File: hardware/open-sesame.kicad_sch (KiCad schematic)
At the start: 33 parts, among them J1 Conn_01x02, J2 Conn_01x06, J3 Conn_01x02, J4 Conn_01x02, J5 Conn_01x02, J6 Conn_01x02, J7 Qwiic_RA, U1 CPC1019N, U2 CPC1019N, U3 CPC1019N

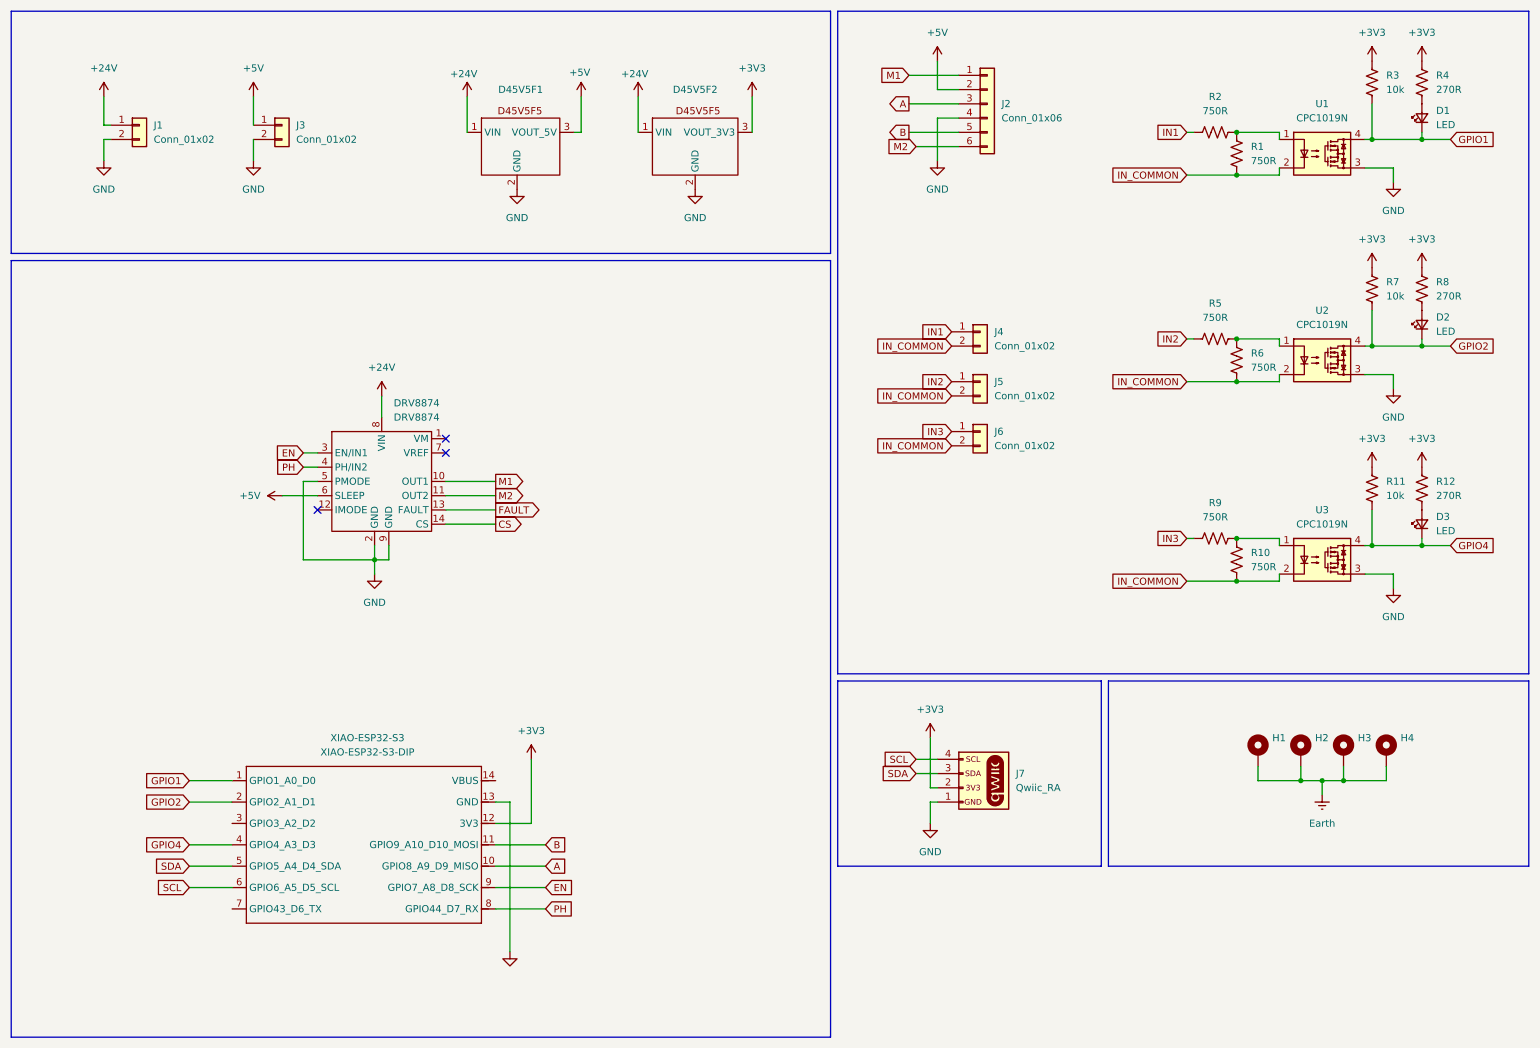
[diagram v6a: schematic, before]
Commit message: hardware: Use screw connectors and PC817
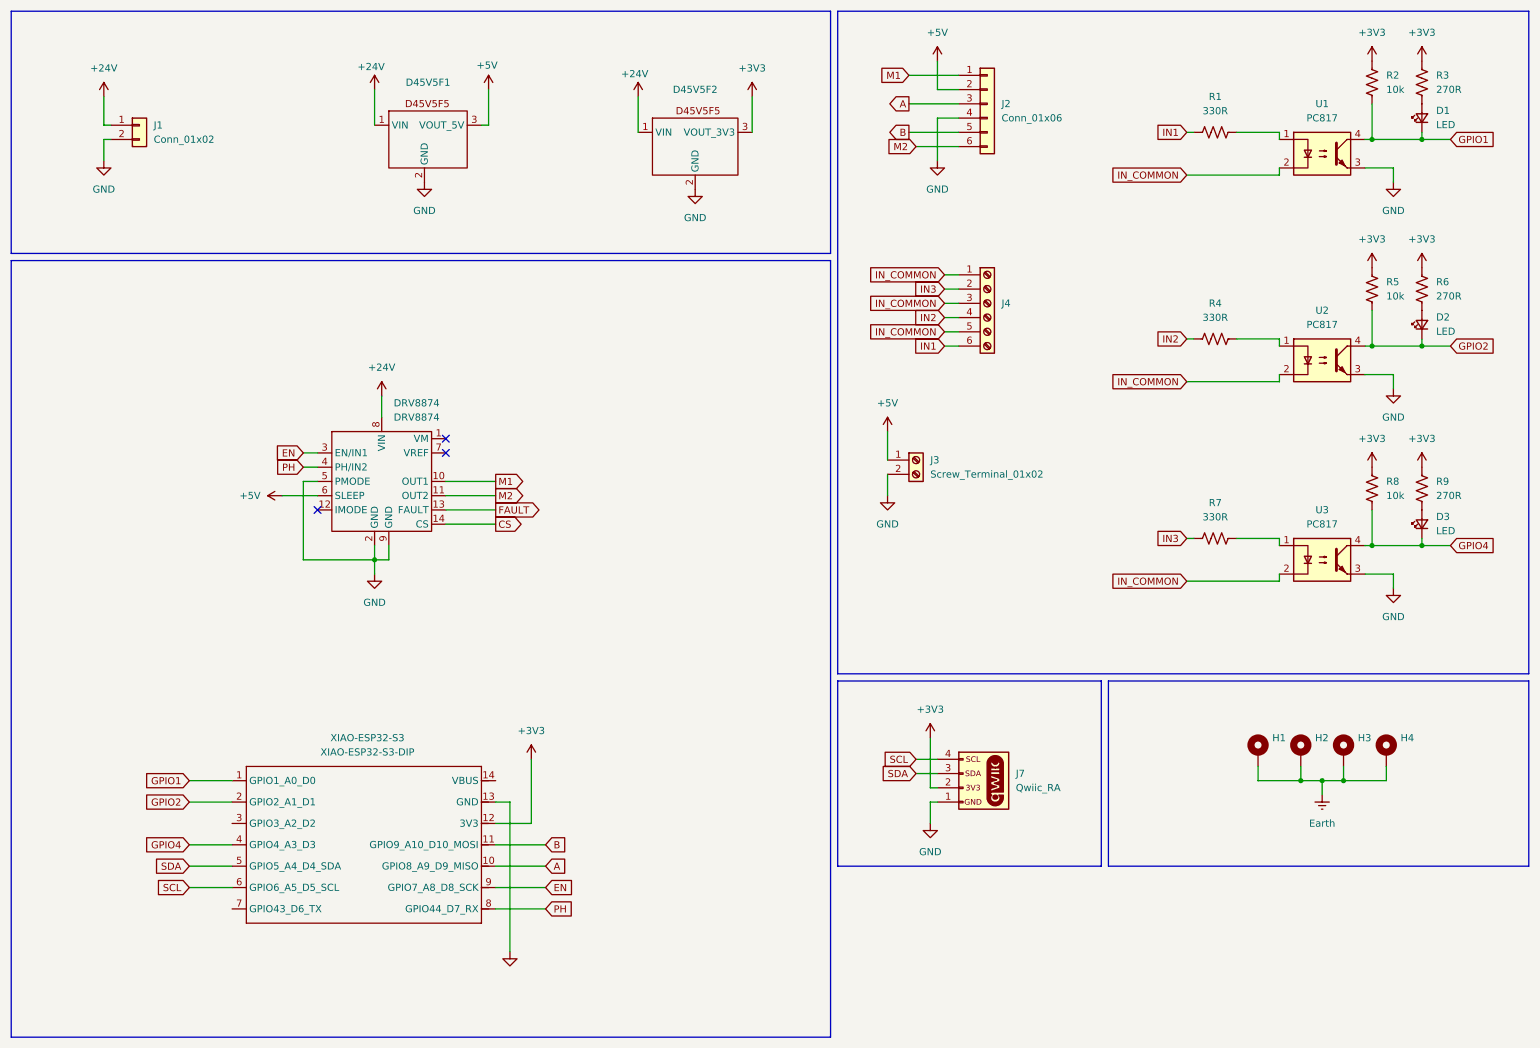
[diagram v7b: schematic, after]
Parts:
- removed J3, J4, J5, J6: Conn_01x02, Connector_Molex:Molex_Nano-Fit_105313-xx02_1x02_P2.50mm_Horizontal, symbol Connector_Generic:Conn_01x02
- removed R10, R2, R5, R6, R9: 750R, Resistor_SMD:R_0603_1608Metric, symbol Device:R_US
- removed U1, U2, U3: CPC1019N, Package_SO:SOP-4_3.8x4.1mm_P2.54mm, symbol Relay_SolidState:CPC1019N
- added J3: Screw_Terminal_01x02, TerminalBlock_Phoenix:TerminalBlock_Phoenix_MPT-0,5-2-2.54_1x02_P2.54mm_Horizontal, symbol Connector:Screw_Terminal_01x02
- added J4: Screw_Terminal_01x06, TerminalBlock_Phoenix:TerminalBlock_Phoenix_MPT-0,5-6-2.54_1x06_P2.54mm_Horizontal, symbol Connector:Screw_Terminal_01x06
- added R4, R7: 330R, Resistor_SMD:R_0603_1608Metric, symbol Device:R_US
- added U1, U2, U3: PC817, Package_DIP:DIP-4_W7.62mm, symbol Isolator:PC817
- R1: value 750R -> 330R
- renumbered R3 to R2, R4 to R3, R7 to R5, R8 to R6, R11 to R8, R12 to R9
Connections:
- net +5V: now also J3.1 (Pin_1)
- net GND: now also J3.2 (Pin_2), U1.3, U2.3, U3.3
- net GPIO1: now also U1.4
- net GPIO2: now also U2.4
- net GPIO4: now also U3.4
- net IN1: now also R1.1, J4.6 (Pin_6)
- net IN2: now also J4.4 (Pin_4), R4.1
- net IN3: now also J4.2 (Pin_2), R7.1
- net IN_COMMON: now also J4.1 (Pin_1), J4.3 (Pin_3), J4.5 (Pin_5), U1.2, U2.2, U3.2; no longer R1.2
- new net: R4.2, U2.1
- new net: R1.2, U1.1
- new net: R7.2, U3.1
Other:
- moved on the sheet: D45V5F1

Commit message: hardware: use one power converter, shrink size, change connectors
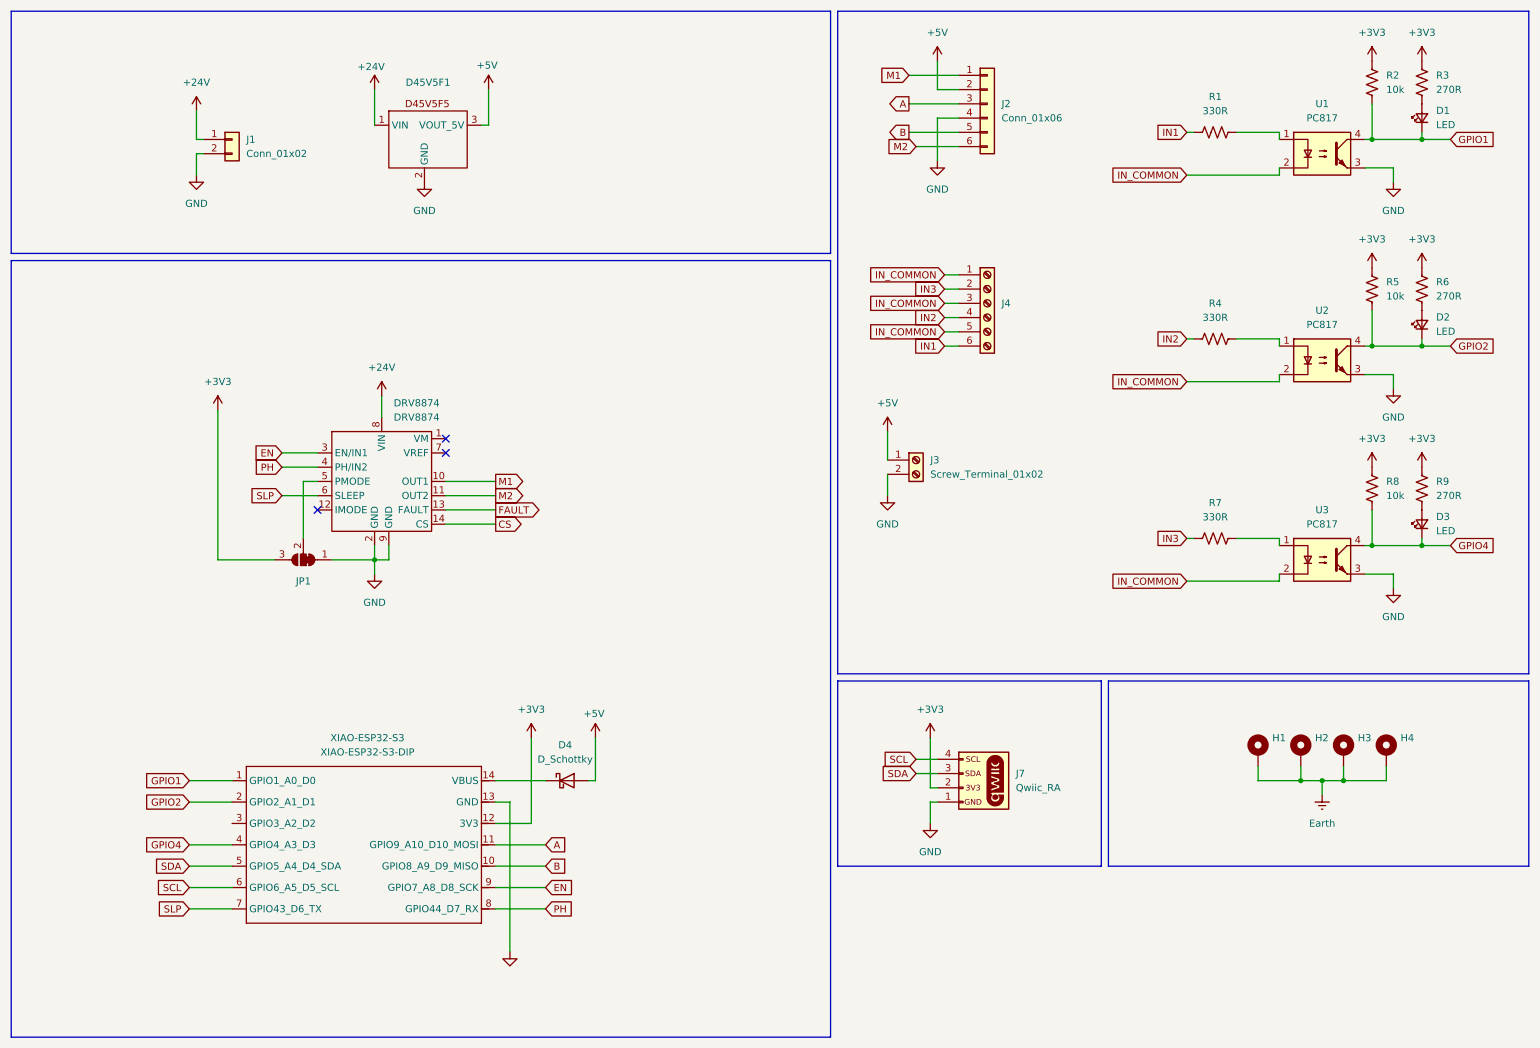
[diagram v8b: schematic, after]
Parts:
- removed D45V5F2: D45V5F3, MyLibrary:D45V5Fx, symbol MyLibrary:D45V5F3
- added D4: D_Schottky, Diode_SMD:D_0603_1608Metric_Pad1.05x0.95mm_HandSolder, symbol Device:D_Schottky
- added JP1: SolderJumper_3_Bridged12, Jumper:SolderJumper-3_P1.3mm_Bridged2Bar12_Pad1.0x1.5mm, symbol Jumper:SolderJumper_3_Bridged12
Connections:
- net +3V3: now also JP1.3 (B)
- net +5V: now also D4.2 (A); no longer DRV8874.6 (SLEEP)
- net A: now also XIAO-ESP32-S3.11 (GPIO9_A10_D10_MOSI); no longer XIAO-ESP32-S3.10 (GPIO8_A9_D9_MISO)
- net B: now also XIAO-ESP32-S3.10 (GPIO8_A9_D9_MISO); no longer XIAO-ESP32-S3.11 (GPIO9_A10_D10_MOSI)
- net GND: now also JP1.1 (A); no longer DRV8874.5 (PMODE)
- net at XIAO-ESP32-S3.14 (VBUS): now also D4.1 (K)
- net SLP: now reaches XIAO-ESP32-S3.7 (GPIO43_D6_TX)
- net SLP: now also DRV8874.6 (SLEEP)
- new net: DRV8874.5 (PMODE), JP1.2 (C)
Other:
- moved on the sheet: J1
